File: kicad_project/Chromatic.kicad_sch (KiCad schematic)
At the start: 159 parts, among them J1 J1, J2 J2

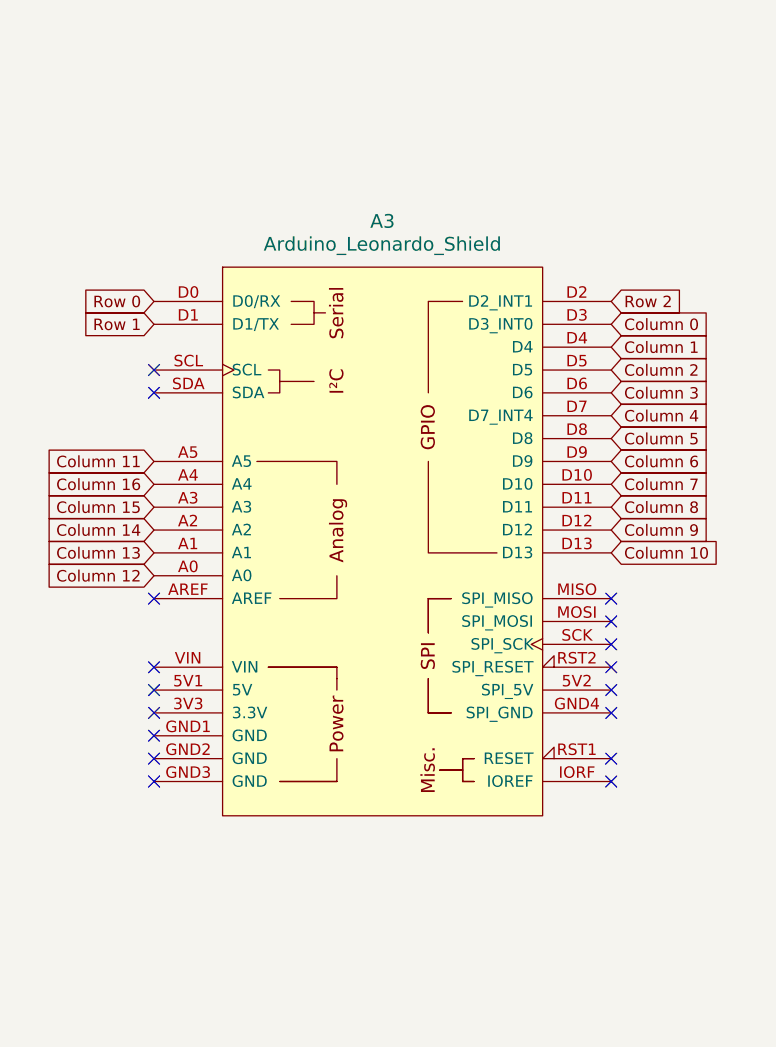
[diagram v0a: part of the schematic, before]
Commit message: TROCADO ARDUINO POR ESP
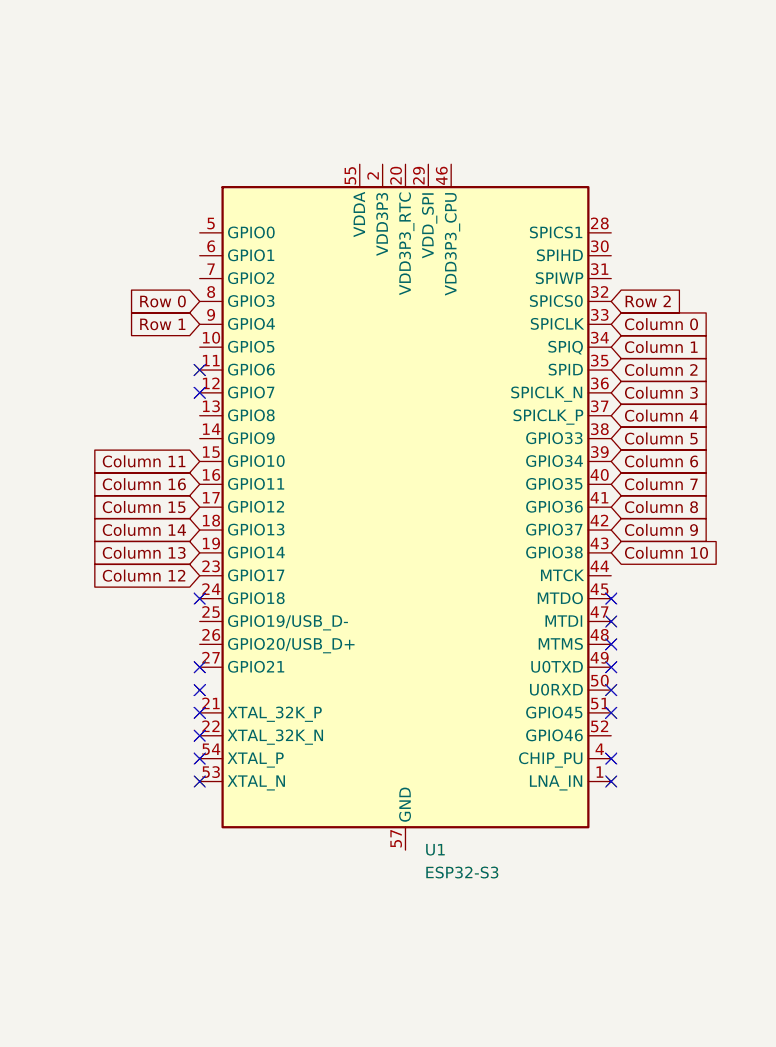
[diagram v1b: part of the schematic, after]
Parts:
- removed A3: Arduino_Leonardo_Shield, Arduino:ARDUINO_A000066, symbol arduino-library:Arduino_Leonardo_Shield
- added U1: ESP32-S3, Module:XCVR_ESP32-S3-DEVKIT-LIPO, symbol MCU_Espressif:ESP32-S3
- D_R0C0, D_R0C1, D_R0C10, D_R0C11, D_R0C12, D_R0C13, D_R0C14, D_R0C15, D_R0C16, D_R0C2, D_R0C3, D_R0C4, D_R0C5, D_R0C6, D_R0C7, D_R0C8, D_R0C9, D_R1C0, D_R1C1, D_R1C10, D_R1C11, D_R1C12, D_R1C13, D_R1C14, D_R1C15, D_R1C16, D_R1C2, D_R1C3, D_R1C4, D_R1C5, D_R1C6, D_R1C7, D_R1C8, D_R1C9, D_R2C0, D_R2C1, D_R2C10, D_R2C11, D_R2C12, D_R2C13, D_R2C14, D_R2C15, D_R2C16, D_R2C2, D_R2C3, D_R2C4, D_R2C5, D_R2C6, D_R2C7, D_R2C8, D_R2C9: value ~ -> (none)
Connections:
- net Column 0: now also U1.33 (SPICLK)
- net Column 1: now also U1.34 (SPIQ)
- net Column 10: now also U1.43 (GPIO38)
- net Column 11: now also U1.15 (GPIO10)
- net Column 12: now also U1.23 (GPIO17)
- net Column 13: now also U1.19 (GPIO14)
- net Column 14: now also U1.18 (GPIO13)
- net Column 15: now also U1.17 (GPIO12)
- net Column 16: now also U1.16 (GPIO11)
- net Column 2: now also U1.35 (SPID)
- net Column 3: now also U1.36 (SPICLK_N)
- net Column 4: now also U1.37 (SPICLK_P)
- net Column 5: now also U1.38 (GPIO33)
- net Column 6: now also U1.39 (GPIO34)
- net Column 7: now also U1.40 (GPIO35)
- net Column 8: now also U1.41 (GPIO36)
- net Column 9: now also U1.42 (GPIO37)
- net Row 0: now also U1.8 (GPIO3)
- net Row 1: now also U1.9 (GPIO4)
- net Row 2: now also U1.32 (SPICS0)
- new net: U1.2 (VDD3P3), U1.3 (VDD3P3)
- new net: U1.55 (VDDA), U1.56 (VDDA)

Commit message: arrumado pcb e footprint
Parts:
- removed D_R0C14, D_R0C15, D_R0C16, D_R1C14, D_R1C15, D_R1C16, D_R2C14, D_R2C15, D_R2C16: (no value), ScottoKeebs_Components:Diode_DO-35, symbol ScottoKeebs:Placeholder_Diode
- removed J1: J1, Connector_PinHeader_2.54mm:PinHeader_1x08_P2.54mm_Vertical, symbol Connector:Conn_01x08_Pin
- removed J2: J2, Connector_PinHeader_2.54mm:PinHeader_1x08_P2.54mm_Vertical, symbol Connector:Conn_01x08_Pin
- removed SW_0_R0C14, SW_0_R0C15, SW_0_R0C16, SW_1_R1C14, SW_1_R1C15, SW_1_R1C16, SW_2_R2C14, SW_2_R2C15, SW_2_R2C16, SW_3_R0C14, SW_3_R0C15, SW_3_R0C16, SW_4_R1C14, SW_4_R1C15, SW_4_R1C16, SW_5_R2C14, SW_5_R2C15, SW_5_R2C16: Keyswitch, ScottoKeebs_Hotswap:Hotswap_MX_1.00u, symbol ScottoKeebs:Placeholder_Keyswitch
- removed U1: ESP32-S3, Module:XCVR_ESP32-S3-DEVKIT-LIPO, symbol MCU_Espressif:ESP32-S3
- added D_R2C17, D_R2C18, D_R2C19, D_R2C20, D_R2C21, D_R2C22, D_R2C23, D_R2C24, D_R2C25, D_R2C26, D_R2C27, D_R2C28, D_R2C29, D_R2C30, D_R2C31, D_R2C32, D_R2C33, D_R2C34, D_R2C35, D_R2C36, D_R2C37, D_R2C38, D_R2C39, D_R2C40, D_R2C41, D_R2C42, D_R2C43, D_R2C44, D_R2C45, D_R2C46, D_R2C47, D_R2C48, D_R2C49, D_R2C50, D_R2C51, D_R2C52, D_R2C53, D_R2C54, D_R2C55, D_R2C56, D_R2C57, D_R2C58: (no value), ScottoKeebs_Components:Diode_DO-35, symbol ScottoKeebs:Placeholder_Diode
- added R3, R4, R5: Resistor, Resistor_THT:R_Axial_DIN0207_L6.3mm_D2.5mm_P7.62mm_Horizontal, symbol ScottoKeebs:Placeholder_Resistor
- added U2: ESP32-S3-DEVKITC-1-N8R8, RF_Module:ESP32-S3-DEVKITC-1-N8R8, symbol ESP32-S3-DEVKITC-1-N8R8:ESP32-S3-DEVKITC-1-N8R8
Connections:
- net D_R0C11 is gone; now on an unnamed net: D_R0C0.1 (K), D_R0C1.1 (K), D_R0C10.1 (K), D_R0C11.1 (K), D_R0C2.1 (K), D_R0C3.1 (K), D_R0C4.1 (K), D_R0C5.1 (K), D_R0C6.1 (K), D_R0C7.1 (K), D_R0C8.1 (K), D_R0C9.1 (K), R0.2
- net D_R1C11 is gone; now on an unnamed net: D_R1C0.1 (K), D_R1C1.1 (K), D_R1C10.1 (K), D_R1C11.1 (K), D_R1C2.1 (K), D_R1C3.1 (K), D_R1C4.1 (K), D_R1C5.1 (K), D_R1C6.1 (K), D_R1C7.1 (K), D_R1C8.1 (K), D_R1C9.1 (K), R1.2
- net D_R2C11 is gone; now on an unnamed net: D_R2C0.1 (K), D_R2C1.1 (K), D_R2C10.1 (K), D_R2C11.1 (K), D_R2C2.1 (K), D_R2C3.1 (K), D_R2C4.1 (K), D_R2C5.1 (K), D_R2C6.1 (K), D_R2C7.1 (K), D_R2C8.1 (K), D_R2C9.1 (K), R2.2
- net Column 0: now also U2.J1_4 (GPIO4)
- net Column 1: now also U2.J1_5 (GPIO5)
- net Column 10: now also SW_0_R0C13.1, SW_1_R1C13.1, SW_2_R2C13.1, SW_3_R0C13.1, SW_4_R1C13.1, SW_5_R2C13.1, U2.J1_14 (GPIO46)
- net Column 11: now also U2.J1_15 (GPIO9)
- net Column 12: now also U2.J1_20 (GPIO14)
- net Column 13: now also U2.J1_19 (GPIO13)
- net Column 14: now also U2.J1_18 (GPIO12)
- net Column 15: now also U2.J1_17 (GPIO11)
- net Column 16: now also U2.J1_16 (GPIO10)
- net Column 2: now also U2.J1_6 (GPIO6)
- net Column 3: now also U2.J1_7 (GPIO7)
- net Column 4: now also U2.J1_8 (GPIO15)
- net Column 5: now also U2.J1_9 (GPIO16)
- net Column 6: now also U2.J1_10 (GPIO17)
- net Column 7: now also U2.J1_11 (GPIO18)
- net Column 8: now also U2.J1_12 (GPIO8)
- net Column 9: now also SW_0_R0C12.1, SW_1_R1C12.1, SW_2_R2C12.1, SW_3_R0C12.1, SW_4_R1C12.1, SW_5_R2C12.1, U2.J1_13 (GPIO3)
- net Row 0: now also U2.J3_3 (U0RXD/GPIO44)
- net Row 1: now also R5.1, U2.J3_4 (GPIO1); no longer R1.1
- net Row 2: now also R1.1, U2.J3_5 (GPIO2); no longer R2.1
- net at D_R1C7.2 (A), SW_1_R1C7.2: no longer SW_4_R1C7.2
- net at D_R0C3.2 (A), SW_0_R0C3.2: no longer SW_3_R0C3.2
- net at D_R2C4.2 (A), SW_2_R2C4.2: no longer SW_5_R2C4.2
- net at D_R1C0.2 (A), SW_1_R1C0.2: no longer SW_4_R1C0.2
- net at D_R2C2.2 (A), SW_2_R2C2.2: no longer SW_5_R2C2.2
- net at D_R0C1.2 (A), SW_0_R0C1.2: no longer SW_3_R0C1.2
- net at D_R1C8.2 (A), SW_1_R1C8.2: no longer SW_4_R1C8.2
- net at D_R1C13.2 (A), SW_1_R1C13.2: no longer SW_4_R1C13.2
- net at D_R2C1.2 (A), SW_2_R2C1.2: no longer SW_5_R2C1.2
- net at D_R2C6.2 (A), SW_2_R2C6.2: no longer SW_5_R2C6.2
- net at D_R2C5.2 (A), SW_2_R2C5.2: no longer SW_5_R2C5.2
- net at D_R1C3.2 (A), SW_1_R1C3.2: no longer SW_4_R1C3.2
- net at D_R2C0.2 (A), SW_2_R2C0.2: no longer SW_5_R2C0.2
- net at D_R1C4.2 (A), SW_1_R1C4.2: no longer SW_4_R1C4.2
- net at D_R2C13.2 (A), SW_2_R2C13.2: no longer SW_5_R2C13.2
- net at D_R0C7.2 (A), SW_0_R0C7.2: no longer SW_3_R0C7.2
- net at D_R0C0.2 (A), SW_0_R0C0.2: no longer SW_3_R0C0.2
- net at D_R1C9.2 (A), SW_1_R1C9.2: no longer SW_4_R1C9.2
- net at D_R1C1.2 (A), SW_1_R1C1.2: no longer SW_4_R1C1.2
- net at D_R0C2.2 (A), SW_0_R0C2.2: no longer SW_3_R0C2.2
- net at D_R1C6.2 (A), SW_1_R1C6.2: no longer SW_4_R1C6.2
- net at D_R0C13.2 (A), SW_0_R0C13.2: no longer SW_3_R0C13.2
- net at D_R0C6.2 (A), SW_0_R0C6.2: no longer SW_3_R0C6.2
- net at D_R0C11.2 (A), SW_0_R0C11.2: no longer SW_3_R0C11.2
- net at D_R1C11.2 (A), SW_1_R1C11.2: no longer SW_4_R1C11.2
- net at D_R1C2.2 (A), SW_1_R1C2.2: no longer SW_4_R1C2.2
- net at D_R2C9.2 (A), SW_2_R2C9.2: no longer SW_5_R2C9.2
- net at D_R2C10.2 (A), SW_2_R2C10.2: no longer SW_5_R2C10.2
- net at D_R2C3.2 (A), SW_2_R2C3.2: no longer SW_5_R2C3.2
- net at D_R1C5.2 (A), SW_1_R1C5.2: no longer SW_4_R1C5.2
- net at D_R0C8.2 (A), SW_0_R0C8.2: no longer SW_3_R0C8.2
- net at D_R2C8.2 (A), SW_2_R2C8.2: no longer SW_5_R2C8.2
- net at D_R0C5.2 (A), SW_0_R0C5.2: no longer SW_3_R0C5.2
- net at D_R0C4.2 (A), SW_0_R0C4.2: no longer SW_3_R0C4.2
- net at D_R2C12.2 (A), SW_2_R2C12.2: no longer SW_5_R2C12.2
- net at D_R2C7.2 (A), SW_2_R2C7.2: no longer SW_5_R2C7.2
- net at D_R0C9.2 (A), SW_0_R0C9.2: no longer SW_3_R0C9.2
- net at D_R0C10.2 (A), SW_0_R0C10.2: no longer SW_3_R0C10.2
- net at D_R2C11.2 (A), SW_2_R2C11.2: no longer SW_5_R2C11.2
- net at D_R1C10.2 (A), SW_1_R1C10.2: no longer SW_4_R1C10.2
- net at D_R1C12.2 (A), SW_1_R1C12.2: no longer SW_4_R1C12.2
- net at D_R0C12.2 (A), SW_0_R0C12.2: no longer SW_3_R0C12.2
- new net: D_R2C44.2 (A), SW_3_R0C3.2
- new net: D_R2C55.2 (A), SW_5_R2C12.2
- new net: D_R2C41.1 (K), D_R2C42.1 (K), D_R2C43.1 (K), D_R2C44.1 (K), D_R2C45.1 (K), D_R2C46.1 (K), D_R2C47.1 (K), D_R2C48.1 (K), D_R2C49.1 (K), D_R2C50.1 (K), D_R2C51.1 (K), D_R2C52.1 (K), D_R2C53.1 (K), D_R2C56.1 (K), R5.2
- new net: D_R2C53.2 (A), SW_3_R0C12.2
- new net: D_R2C17.1 (K), D_R2C18.1 (K), D_R2C19.1 (K), D_R2C20.1 (K), D_R2C21.1 (K), D_R2C22.1 (K), D_R2C23.1 (K), D_R2C24.1 (K), D_R2C25.1 (K), D_R2C26.1 (K), D_R2C27.1 (K), D_R2C28.1 (K), D_R2C55.1 (K), D_R2C58.1 (K), R3.2
- new net: D_R2C50.2 (A), SW_3_R0C9.2
- new net: D_R2C37.2 (A), SW_4_R1C8.2
- new net: D_R2C22.2 (A), SW_5_R2C5.2
- new net: D_R2C56.2 (A), SW_3_R0C13.2
- new net: D_R2C43.2 (A), SW_3_R0C2.2
- new net: D_R2C29.1 (K), D_R2C30.1 (K), D_R2C31.1 (K), D_R2C32.1 (K), D_R2C33.1 (K), D_R2C34.1 (K), D_R2C35.1 (K), D_R2C36.1 (K), D_R2C37.1 (K), D_R2C38.1 (K), D_R2C39.1 (K), D_R2C40.1 (K), D_R2C54.1 (K), D_R2C57.1 (K), R4.2
- new net: D_R2C33.2 (A), SW_4_R1C4.2
- new net: D_R2C38.2 (A), SW_4_R1C9.2
- new net: D_R2C36.2 (A), SW_4_R1C7.2
- new net: D_R2C41.2 (A), SW_3_R0C0.2
- new net: D_R2C23.2 (A), SW_5_R2C6.2
- new net: D_R2C32.2 (A), SW_4_R1C3.2
- new net: D_R2C42.2 (A), SW_3_R0C1.2
- new net: D_R2C52.2 (A), SW_3_R0C11.2
- new net: D_R2C25.2 (A), SW_5_R2C8.2
- new net: D_R2C29.2 (A), SW_4_R1C0.2
- new net: D_R2C34.2 (A), SW_4_R1C5.2
- new net: D_R2C27.2 (A), SW_5_R2C10.2
- new net: D_R2C19.2 (A), SW_5_R2C2.2
- new net: D_R2C31.2 (A), SW_4_R1C2.2
- new net: D_R2C48.2 (A), SW_3_R0C7.2
- new net: D_R2C51.2 (A), SW_3_R0C10.2
- new net: D_R2C49.2 (A), SW_3_R0C8.2
- new net: D_R2C46.2 (A), SW_3_R0C5.2
- new net: D_R2C58.2 (A), SW_5_R2C13.2
- new net: D_R2C17.2 (A), SW_5_R2C0.2
- new net: D_R2C21.2 (A), SW_5_R2C4.2
- new net: D_R2C39.2 (A), SW_4_R1C10.2
- new net: D_R2C18.2 (A), SW_5_R2C1.2
- new net: D_R2C24.2 (A), SW_5_R2C7.2
- new net: D_R2C30.2 (A), SW_4_R1C1.2
- new net: D_R2C47.2 (A), SW_3_R0C6.2
- new net: D_R2C45.2 (A), SW_3_R0C4.2
- new net: D_R2C40.2 (A), SW_4_R1C11.2
- new net: D_R2C57.2 (A), SW_4_R1C13.2
- new net: D_R2C20.2 (A), SW_5_R2C3.2
- new net: D_R2C26.2 (A), SW_5_R2C9.2
- new net: D_R2C54.2 (A), SW_4_R1C12.2
- new net: D_R2C28.2 (A), SW_5_R2C11.2
- new net: D_R2C35.2 (A), SW_4_R1C6.2
- new net Row 3: R4.1, U2.J3_16 (GPIO48)
- new net Row 4: R2.1, U2.J3_17 (GPIO47)
- new net Row 5: R3.1, U2.J3_18 (GPIO21)
- no-connect marks 17 -> 0
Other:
- moved on the sheet: D_R0C0, D_R0C1, D_R0C10, D_R0C11, D_R0C2, D_R0C3, D_R0C4, D_R0C5, D_R0C6, D_R0C7, D_R0C8, D_R0C9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
